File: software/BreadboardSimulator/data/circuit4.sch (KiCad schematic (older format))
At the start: 4 parts, among them U1-8 8pinChip

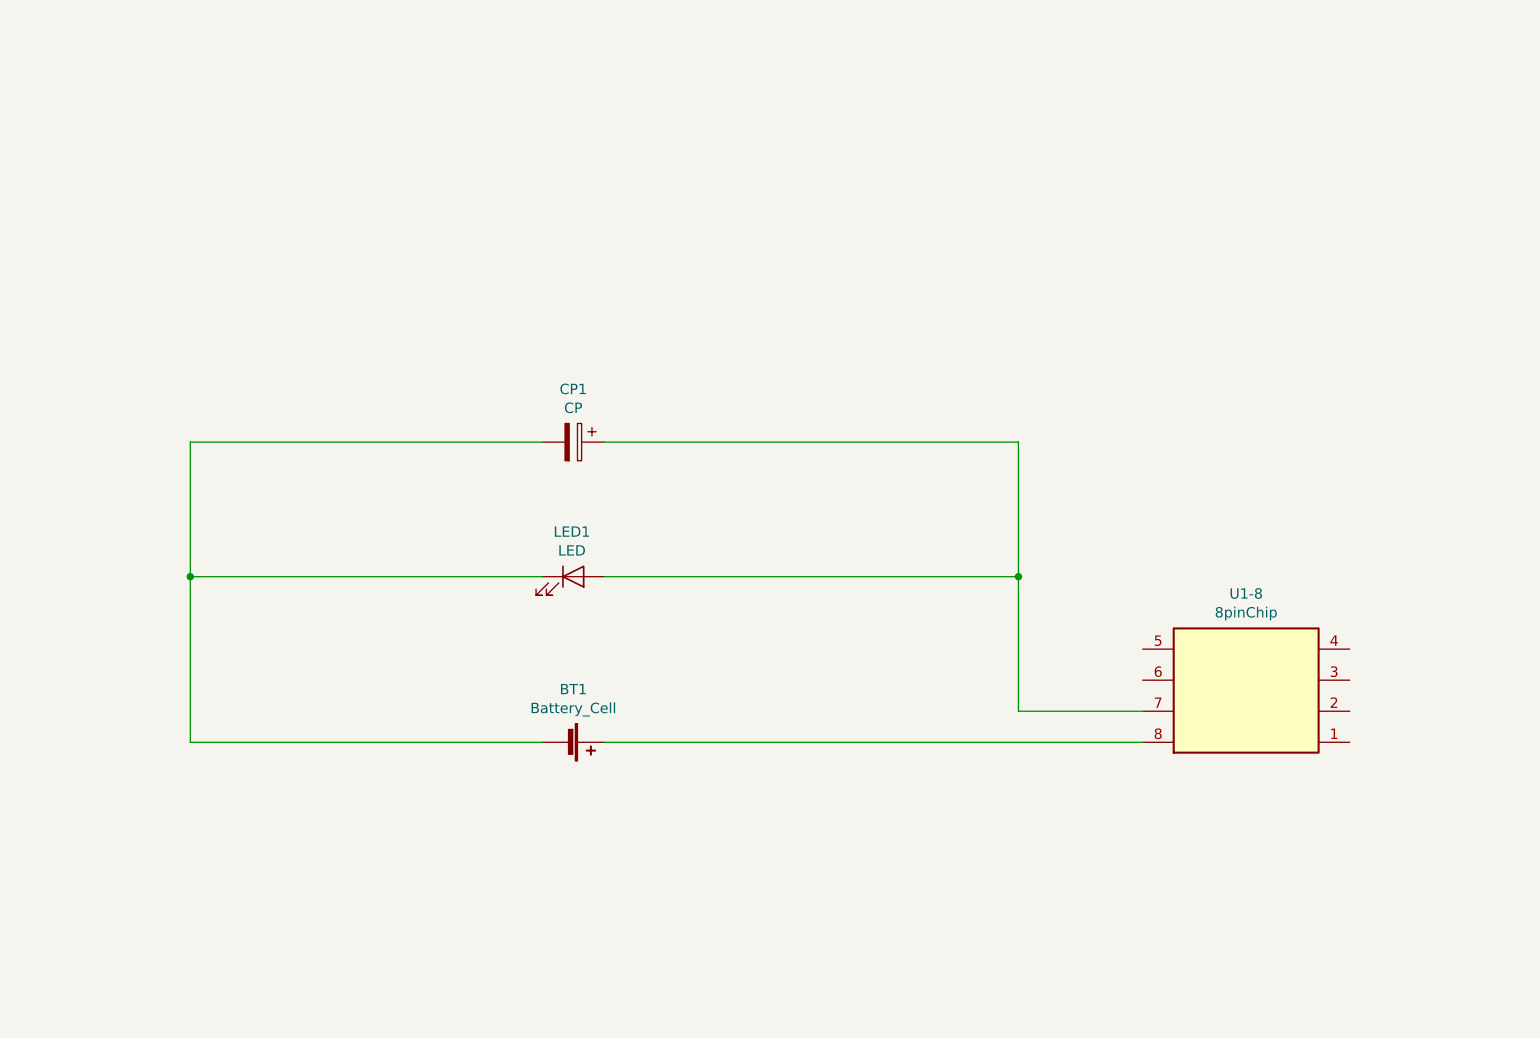
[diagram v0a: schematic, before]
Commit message: Bugfix change to find index of '-' for having last index of '-' (chips)
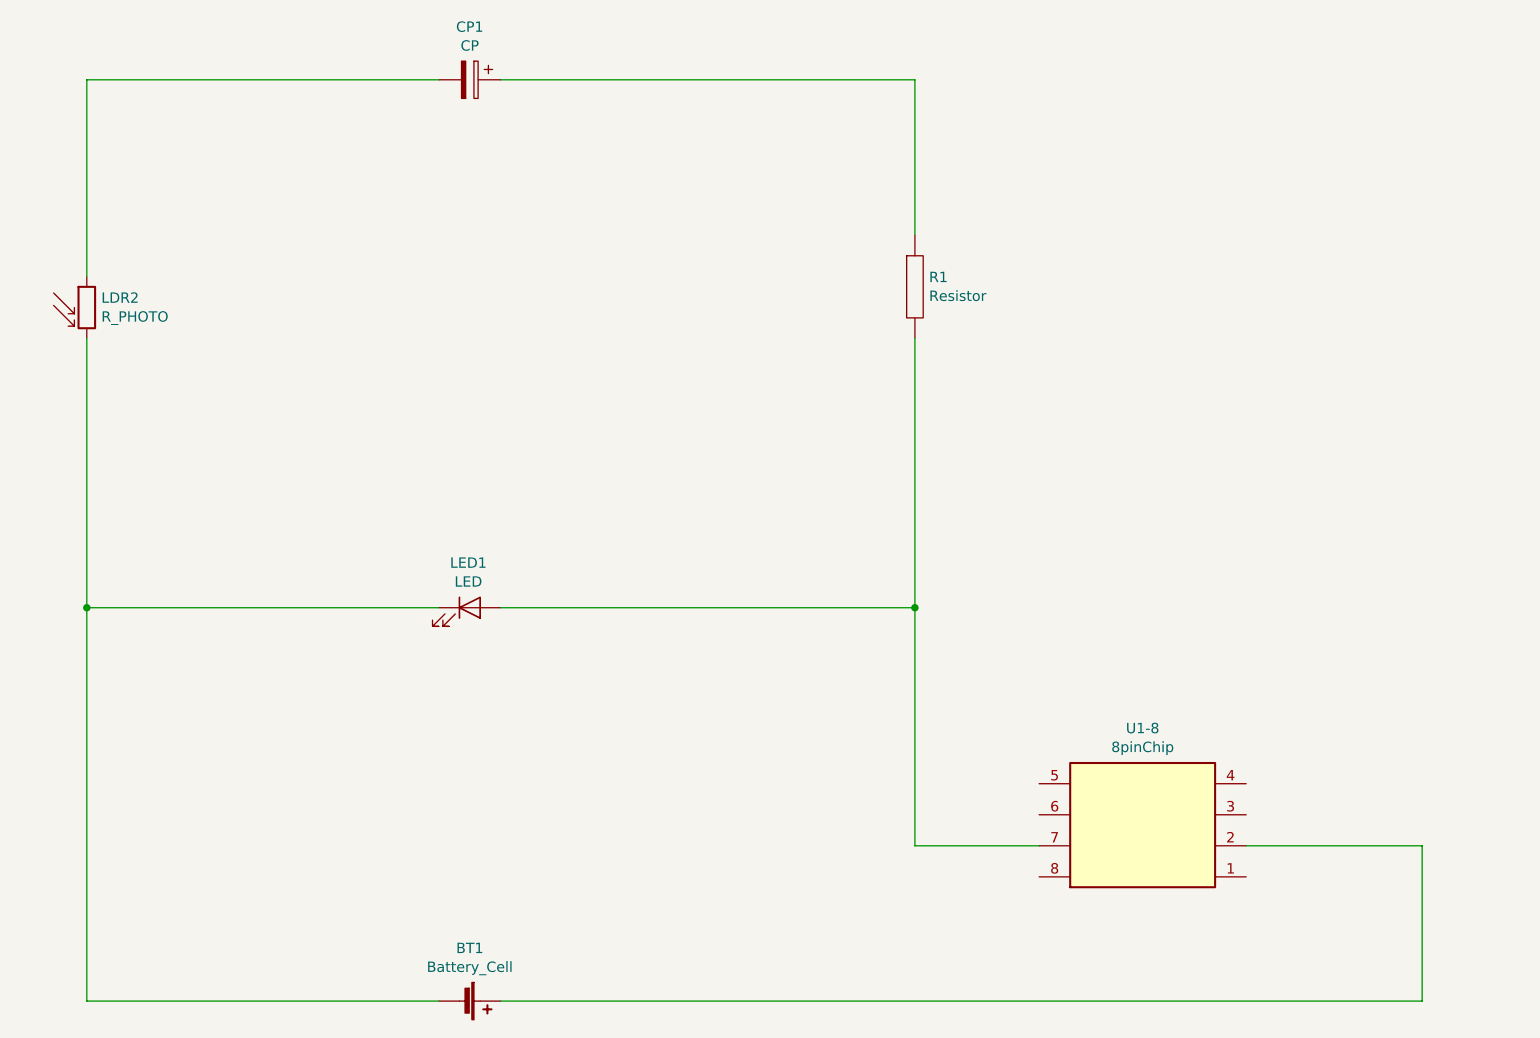
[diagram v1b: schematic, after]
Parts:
- added LDR2: R_PHOTO, symbol SchemaBoard_Library:R_PHOTO
- added R1: Resistor, symbol SchemaBoard_Library:Resistor
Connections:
- net at U1-8.2: now also BT1.1 (+)
- net at LED1.2 (A), U1-8.7: now also R1.2; no longer CP1.1
- net at U1-8.8: no longer BT1.1 (+)
- net at BT1.2 (-), LED1.1 (K): now also LDR2.2; no longer CP1.2
- new net: CP1.2, LDR2.1
- new net: CP1.1, R1.1
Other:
- moved on the sheet: BT1, CP1, LED1, U1-8
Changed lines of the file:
@@
 EESchema Schematic File Version 4
-LIBS:circuit3-cache
+LIBS:circuit4-cache
 EELAYER 29 0
 EELAYER END
@@
 L SchemaBoard_Library:8pinChip U1-8
 U 1 1 5D4536D3
-P 6750 4250
-F 0 "U1-8" H 6750 4717 50  0000 C CNN
-F 1 "8pinChip" H 6750 4626 50  0000 C CNN
-F 2 "" H 6750 4250 50  0001 C CNN
-F 3 "http://www.ti.com/lit/ds/symlink/lm555.pdf" H 6750 4250 50  0001 C CNN
-	1    6750 4250
+P 6250 4900
+F 0 "U1-8" H 6250 5367 50  0000 C CNN
+F 1 "8pinChip" H 6250 5276 50  0000 C CNN
+F 2 "" H 6250 4900 50  0001 C CNN
+F 3 "http://www.ti.com/lit/ds/symlink/lm555.pdf" H 6250 4900 50  0001 C CNN
+	1    6250 4900
 	1    0    0    -1
 $EndComp
@@
 L SchemaBoard_Library:LED LED1
 U 1 1 5D4552BA
-P 3500 3700
-F 0 "LED1" H 3493 3916 50  0000 C CNN
-F 1 "LED" H 3493 3825 50  0000 C CNN
-F 2 "" H 3500 3700 50  0001 C CNN
-F 3 "~" H 3500 3700 50  0001 C CNN
-	1    3500 3700
+P 3000 3850
+F 0 "LED1" H 2993 4066 50  0000 C CNN
+F 1 "LED" H 2993 3975 50  0000 C CNN
+F 2 "" H 3000 3850 50  0001 C CNN
+F 3 "~" H 3000 3850 50  0001 C CNN
+	1    3000 3850
 	1    0    0    -1
 $EndComp
@@
 L SchemaBoard_Library:Battery_Cell BT1
 U 1 1 5D455990
-P 3450 4500
-F 0 "BT1" V 3195 4550 50  0000 C CNN
-F 1 "Battery_Cell" V 3286 4550 50  0000 C CNN
-F 2 "" V 3450 4560 50  0001 C CNN
-F 3 "~" V 3450 4560 50  0001 C CNN
-	1    3450 4500
+P 2950 5750
+F 0 "BT1" V 2695 5800 50  0000 C CNN
+F 1 "Battery_Cell" V 2786 5800 50  0000 C CNN
+F 2 "" V 2950 5810 50  0001 C CNN
+F 3 "~" V 2950 5810 50  0001 C CNN
+	1    2950 5750
+	0    1    1    0
+$EndComp
+$Comp
+L SchemaBoard_Library:CP CP1
+U 1 1 5D45475C
+P 3000 1300
+F 0 "CP1" V 2745 1300 50  0000 C CNN
+F 1 "CP" V 2836 1300 50  0000 C CNN
+F 2 "" H 3038 1150 50  0001 C CNN
+F 3 "~" H 3000 1300 50  0001 C CNN
+	1    3000 1300
 	0    1    1    0
 $EndComp
 Wire Wire Line
-	6250 4500 3650 4500
+	5150 5000 5750 5000
 Wire Wire Line
-	1650 4500 1650 3700
+	2850 5750 1150 5750
+Wire Wire Line
+	1150 1300 2850 1300
+Wire Wire Line
+	3150 1300 5150 1300
+Wire Wire Line
+	1150 3850 2850 3850
+Wire Wire Line
+	3150 3850 5150 3850
 $Comp
-L SchemaBoard_Library:CP CP1
-U 1 1 5D45475C
-P 3500 3050
-F 0 "CP1" V 3245 3050 50  0000 C CNN
-F 1 "CP" V 3336 3050 50  0000 C CNN
-F 2 "" H 3538 2900 50  0001 C CNN
-F 3 "~" H 3500 3050 50  0001 C CNN
-	1    3500 3050
-	0    1    1    0
+L SchemaBoard_Library:R_PHOTO LDR2
+U 1 1 5D4244B8
+P 1150 2400
+F 0 "LDR2" H 1220 2446 50  0000 L CNN
+F 1 "R_PHOTO" H 1220 2355 50  0000 L CNN
+F 2 "" V 1200 2150 50  0001 L CNN
+F 3 "~" H 1150 2350 50  0001 C CNN
+	1    1150 2400
+	1    0    0    -1
+$EndComp
+$Comp
+L SchemaBoard_Library:Resistor R1
+U 1 1 5D42507A
+P 5150 2300
+F 0 "R1" H 5218 2346 50  0000 L CNN
+F 1 "Resistor" H 5218 2255 50  0000 L CNN
+F 2 "" H 5150 2300 50  0001 C CNN
+F 3 "~" H 5150 2300 50  0001 C CNN
+	1    5150 2300
+	1    0    0    -1
 $EndComp
 Wire Wire Line
-	5650 4350 6250 4350
+	5150 1300 5150 2050
 Wire Wire Line
-	3350 4500 1650 4500
+	1150 1300 1150 2250
 Wire Wire Line
-	1650 3050 3350 3050
-Connection ~ 1650 3700
+	7600 5000 6750 5000
 Wire Wire Line
-	1650 3700 1650 3050
+	3150 5750 7600 5750
+Connection ~ 1150 3850
 Wire Wire Line
-	3650 3050 5650 3050
+	1150 2550 1150 3850
 Wire Wire Line
-	1650 3700 3350 3700
+	5150 2550 5150 3850
 Wire Wire Line
-	5650 3050 5650 3700
+	1150 3850 1150 5750
 Wire Wire Line
-	3650 3700 5650 3700
-Connection ~ 5650 3700
+	5150 3850 5150 5000
 Wire Wire Line
-	5650 3700 5650 4350
+	7600 5000 7600 5750
+Connection ~ 5150 3850
 $EndSCHEMATC

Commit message: Bugfix add connectors for update wires' position when drag the component (chip)
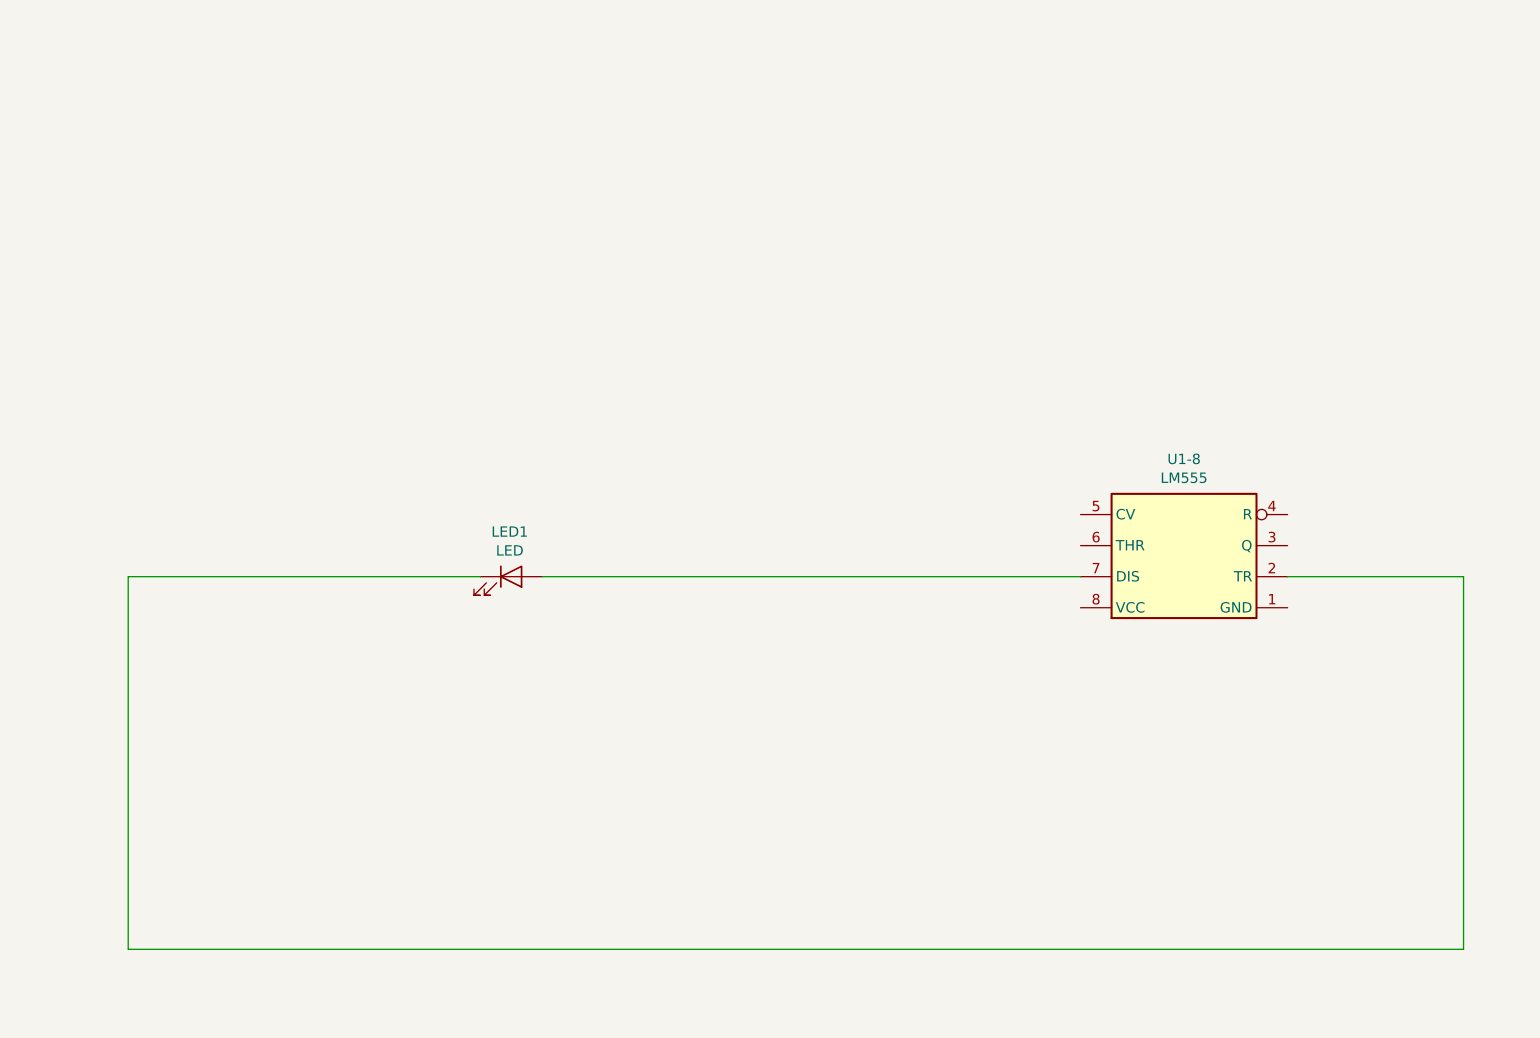
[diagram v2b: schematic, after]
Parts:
- removed BT1: Battery_Cell, symbol SchemaBoard_Library:Battery_Cell
- removed CP1: CP, symbol SchemaBoard_Library:CP
- removed LDR2: R_PHOTO, symbol SchemaBoard_Library:R_PHOTO
- removed R1: Resistor, symbol SchemaBoard_Library:Resistor
- removed U1-8: 8pinChip, symbol SchemaBoard_Library:8pinChip
- added U1-8: LM555, symbol SchemaBoard_Library:LM555
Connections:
- net at LED1.1 (K): now also U1-8.2 (TR)
- net at LED1.2 (A): now also U1-8.7 (DIS)
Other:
- moved on the sheet: LED1
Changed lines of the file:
@@
 $EndDescr
-$Comp
-L SchemaBoard_Library:8pinChip U1-8
-U 1 1 5D4536D3
-P 6250 4900
-F 0 "U1-8" H 6250 5367 50  0000 C CNN
-F 1 "8pinChip" H 6250 5276 50  0000 C CNN
-F 2 "" H 6250 4900 50  0001 C CNN
-F 3 "http://www.ti.com/lit/ds/symlink/lm555.pdf" H 6250 4900 50  0001 C CNN
-	1    6250 4900
-	1    0    0    -1
-$EndComp
 $Comp
 L SchemaBoard_Library:LED LED1
 U 1 1 5D4552BA
-P 3000 3850
-F 0 "LED1" H 2993 4066 50  0000 C CNN
-F 1 "LED" H 2993 3975 50  0000 C CNN
-F 2 "" H 3000 3850 50  0001 C CNN
-F 3 "~" H 3000 3850 50  0001 C CNN
-	1    3000 3850
-	1    0    0    -1
-$EndComp
-$Comp
-L SchemaBoard_Library:Battery_Cell BT1
-U 1 1 5D455990
-P 2950 5750
-F 0 "BT1" V 2695 5800 50  0000 C CNN
-F 1 "Battery_Cell" V 2786 5800 50  0000 C CNN
-F 2 "" V 2950 5810 50  0001 C CNN
-F 3 "~" V 2950 5810 50  0001 C CNN
-	1    2950 5750
-	0    1    1    0
-$EndComp
-$Comp
-L SchemaBoard_Library:CP CP1
-U 1 1 5D45475C
-P 3000 1300
-F 0 "CP1" V 2745 1300 50  0000 C CNN
-F 1 "CP" V 2836 1300 50  0000 C CNN
-F 2 "" H 3038 1150 50  0001 C CNN
-F 3 "~" H 3000 1300 50  0001 C CNN
-	1    3000 1300
-	0    1    1    0
-$EndComp
-Wire Wire Line
-	5150 5000 5750 5000
-Wire Wire Line
-	2850 5750 1150 5750
-Wire Wire Line
-	1150 1300 2850 1300
-Wire Wire Line
-	3150 1300 5150 1300
-Wire Wire Line
-	1150 3850 2850 3850
-Wire Wire Line
-	3150 3850 5150 3850
-$Comp
-L SchemaBoard_Library:R_PHOTO LDR2
-U 1 1 5D4244B8
-P 1150 2400
-F 0 "LDR2" H 1220 2446 50  0000 L CNN
-F 1 "R_PHOTO" H 1220 2355 50  0000 L CNN
-F 2 "" V 1200 2150 50  0001 L CNN
-F 3 "~" H 1150 2350 50  0001 C CNN
-	1    1150 2400
-	1    0    0    -1
-$EndComp
-$Comp
-L SchemaBoard_Library:Resistor R1
-U 1 1 5D42507A
-P 5150 2300
-F 0 "R1" H 5218 2346 50  0000 L CNN
-F 1 "Resistor" H 5218 2255 50  0000 L CNN
-F 2 "" H 5150 2300 50  0001 C CNN
-F 3 "~" H 5150 2300 50  0001 C CNN
-	1    5150 2300
+P 3200 3700
+F 0 "LED1" H 3193 3916 50  0000 C CNN
+F 1 "LED" H 3193 3825 50  0000 C CNN
+F 2 "" H 3200 3700 50  0001 C CNN
+F 3 "~" H 3200 3700 50  0001 C CNN
+	1    3200 3700
 	1    0    0    -1
 $EndComp
 Wire Wire Line
-	5150 1300 5150 2050
+	1350 3700 3050 3700
 Wire Wire Line
-	1150 1300 1150 2250
+	7800 3700 6950 3700
+$Comp
+L SchemaBoard_Library:LM555 U1-8
+U 1 1 5D433B16
+P 6450 3600
+F 0 "U1-8" H 6450 4067 50  0000 C CNN
+F 1 "LM555" H 6450 3976 50  0000 C CNN
+F 2 "" H 6450 3600 50  0001 C CNN
+F 3 "http://www.ti.com/lit/ds/symlink/lm555.pdf" H 6450 3600 50  0001 C CNN
+	1    6450 3600
+	1    0    0    -1
+$EndComp
 Wire Wire Line
-	7600 5000 6750 5000
+	1350 5500 7800 5500
 Wire Wire Line
-	3150 5750 7600 5750
-Connection ~ 1150 3850
+	7800 3700 7800 5500
 Wire Wire Line
-	1150 2550 1150 3850
+	1350 3700 1350 5500
 Wire Wire Line
-	5150 2550 5150 3850
-Wire Wire Line
-	1150 3850 1150 5750
-Wire Wire Line
-	5150 3850 5150 5000
-Wire Wire Line
-	7600 5000 7600 5750
-Connection ~ 5150 3850
+	3350 3700 5950 3700
 $EndSCHEMATC

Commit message: In progress: travel net lists
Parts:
- added CP1: CP, symbol SchemaBoard_Library:CP
- added GND1, GND2: GND, symbol SchemaBoard_Library:GND
- added LED2: LED, symbol SchemaBoard_Library:LED
- added PWR1, PWR2: +3V3, symbol SchemaBoard_Library:+3V3
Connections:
- wire segments 6 -> 18
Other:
- moved on the sheet: LED1
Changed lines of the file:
@@
 L SchemaBoard_Library:LED LED1
 U 1 1 5D4552BA
-P 3200 3700
-F 0 "LED1" H 3193 3916 50  0000 C CNN
-F 1 "LED" H 3193 3825 50  0000 C CNN
-F 2 "" H 3200 3700 50  0001 C CNN
-F 3 "~" H 3200 3700 50  0001 C CNN
-	1    3200 3700
+P 6500 4850
+F 0 "LED1" H 6493 5066 50  0000 C CNN
+F 1 "LED" H 6493 4975 50  0000 C CNN
+F 2 "" H 6500 4850 50  0001 C CNN
+F 3 "~" H 6500 4850 50  0001 C CNN
+	1    6500 4850
+	1    0    0    -1
+$EndComp
+$Comp
+L SchemaBoard_Library:+3V3 PWR1
+U 1 1 5D438B69
+P 1400 4500
+F 0 "PWR1" H 1400 4350 50  0001 C CNN
+F 1 "+3V3" H 1488 4537 50  0000 L CNN
+F 2 "" H 1400 4500 50  0001 C CNN
+F 3 "" H 1400 4500 50  0001 C CNN
+	1    1400 4500
+	1    0    0    -1
+$EndComp
+$Comp
+L SchemaBoard_Library:GND GND1
+U 1 1 5D439298
+P 5800 5750
+F 0 "GND1" H 5800 5500 50  0001 C CNN
+F 1 "GND" H 5888 5713 50  0000 L CNN
+F 2 "" H 5800 5750 50  0001 C CNN
+F 3 "" H 5800 5750 50  0001 C CNN
+	1    5800 5750
+	1    0    0    -1
+$EndComp
+$Comp
+L SchemaBoard_Library:GND GND2
+U 1 1 5D439F46
+P 3300 3600
+F 0 "GND2" H 3300 3350 50  0001 C CNN
+F 1 "GND" H 3388 3563 50  0000 L CNN
+F 2 "" H 3300 3600 50  0001 C CNN
+F 3 "" H 3300 3600 50  0001 C CNN
+	1    3300 3600
+	1    0    0    -1
+$EndComp
+$Comp
+L SchemaBoard_Library:LM555 U1-8
+U 1 1 5D43A409
+P 3900 5050
+F 0 "U1-8" H 3900 5517 50  0000 C CNN
+F 1 "LM555" H 3900 5426 50  0000 C CNN
+F 2 "" H 3900 5050 50  0001 C CNN
+F 3 "http://www.ti.com/lit/ds/symlink/lm555.pdf" H 3900 5050 50  0001 C CNN
+	1    3900 5050
 	1    0    0    -1
 $EndComp
 Wire Wire Line
-	1350 3700 3050 3700
-Wire Wire Line
-	7800 3700 6950 3700
+	5800 5300 5800 5750
 $Comp
-L SchemaBoard_Library:LM555 U1-8
-U 1 1 5D433B16
-P 6450 3600
-F 0 "U1-8" H 6450 4067 50  0000 C CNN
-F 1 "LM555" H 6450 3976 50  0000 C CNN
-F 2 "" H 6450 3600 50  0001 C CNN
-F 3 "http://www.ti.com/lit/ds/symlink/lm555.pdf" H 6450 3600 50  0001 C CNN
-	1    6450 3600
+L SchemaBoard_Library:+3V3 PWR2
+U 1 1 5D440E67
+P 7500 4400
+F 0 "PWR2" H 7500 4250 50  0001 C CNN
+F 1 "+3V3" H 7588 4437 50  0000 L CNN
+F 2 "" H 7500 4400 50  0001 C CNN
+F 3 "" H 7500 4400 50  0001 C CNN
+	1    7500 4400
 	1    0    0    -1
 $EndComp
 Wire Wire Line
-	1350 5500 7800 5500
+	7500 4400 7500 4850
 Wire Wire Line
-	7800 3700 7800 5500
+	7500 4850 7100 4850
+$Comp
+L SchemaBoard_Library:CP CP1
+U 1 1 5D438166
+P 6500 3250
+F 0 "CP1" V 6245 3250 50  0000 C CNN
+F 1 "CP" V 6336 3250 50  0000 C CNN
+F 2 "" H 6538 3100 50  0001 C CNN
+F 3 "~" H 6500 3250 50  0001 C CNN
+	1    6500 3250
+	0    1    1    0
+$EndComp
 Wire Wire Line
-	1350 3700 1350 5500
+	6650 3250 7100 3250
 Wire Wire Line
-	3350 3700 5950 3700
+	7100 3250 7100 4850
+Connection ~ 7100 4850
+Wire Wire Line
+	7100 4850 6650 4850
+Wire Wire Line
+	6350 3250 5600 3250
+Wire Wire Line
+	5600 3250 5600 4850
+Wire Wire Line
+	5600 4850 6350 4850
+$Comp
+L SchemaBoard_Library:LED LED2
+U 1 1 5D44AD88
+P 4300 2500
+F 0 "LED2" H 4293 2716 50  0000 C CNN
+F 1 "LED" H 4293 2625 50  0000 C CNN
+F 2 "" H 4300 2500 50  0001 C CNN
+F 3 "~" H 4300 2500 50  0001 C CNN
+	1    4300 2500
+	1    0    0    -1
+$EndComp
+Wire Wire Line
+	4450 2500 5450 2500
+Wire Wire Line
+	5450 2500 5450 5000
+Wire Wire Line
+	4400 5300 5800 5300
+Wire Wire Line
+	4400 5000 5450 5000
+Wire Wire Line
+	4400 4850 5600 4850
+Connection ~ 5600 4850
+Wire Wire Line
+	4150 2500 3300 2500
+Wire Wire Line
+	3300 2500 3300 3600
+Wire Wire Line
+	1400 4500 1400 5300
+Wire Wire Line
+	1400 5300 3400 5300
 $EndSCHEMATC
